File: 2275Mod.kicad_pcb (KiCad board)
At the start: 2 copper layers, 6 parts, among them J1 640388-8, J200 Conn_PIC_ICSP_ICD, K1 4052, K2 G5LE-14-CF_DC24, U1 LM340LAZ-5.0

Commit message: commit before starting kicad 7
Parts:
- added C1: .01/400v, Capacitor_THT:C_Rect_L10.0mm_W4.0mm_P7.50mm_MKS4, F.Cu at (118.2, 93.1)
- added C2: 1000uf, Capacitor_THT:CP_Radial_D16.0mm_P7.50mm, F.Cu at (146.6, 80.0)
- added C200: .1uf, Capacitor_SMD:C_0603_1608Metric_Pad1.08x0.95mm_HandSolder, F.Cu at (195.1, 97.0)
- added C201: 4700uf, Capacitor_THT:CP_Radial_D25.0mm_P10.00mm_SnapIn, F.Cu at (203.9, 114.8)
- added C3: 10uf, Capacitor_THT:CP_Radial_D5.0mm_P2.50mm, F.Cu at (187.5, 97.0)
- added D1: MRA4007T3G, Diode_SMD:D_SMA, F.Cu at (143.3, 100.6)
- added D200: LED, LED_SMD:LED_0603_1608Metric_Pad1.05x0.95mm_HandSolder, F.Cu at (188.5, 78.7)
- added D201: LED, LED_SMD:LED_0805_2012Metric_Pad1.15x1.40mm_HandSolder, F.Cu at (188.5, 83.1)
- added H1: MountingHole, MountingHole:MountingHole_3.7mm, F.Cu at (108.2, 122.4)
- added H2: MountingHole, MountingHole:MountingHole_3.7mm, F.Cu at (206.8, 96.8)
- added H3: MountingHole, MountingHole:MountingHole_3.7mm, F.Cu at (108.2, 77.7)
- added IC1: LTV-356T, AAA_JH:SOP254P675X220-4N, F.Cu at (135.9, 87.9)
- added J201: Conn_01x03_Male, Connector_PinHeader_2.54mm:PinHeader_1x03_P2.54mm_Vertical, F.Cu at (196.1, 80.5)
- added Q200: Q_NPN_Darlington_CBE, AAA_JH:TRANS_2SD1918_ROM-M, F.Cu at (205.5, 79.2)
- added Q201: Q_NPN_Darlington_CBE, AAA_JH:TRANS_2SD1918_ROM-M, F.Cu at (214.9, 79.2)
- added R1: 47, Resistor_SMD:R_0805_2012Metric_Pad1.20x1.40mm_HandSolder, F.Cu at (118.4, 88.4)
- added R2: 2.2k, Resistor_SMD:R_0603_1608Metric_Pad0.98x0.95mm_HandSolder, F.Cu at (126.9, 87.4)
- added R200: 2.2k, Resistor_SMD:R_0603_1608Metric_Pad0.98x0.95mm_HandSolder, F.Cu at (174.8, 85.9)
- added R201: 2.2k, Resistor_SMD:R_0603_1608Metric_Pad0.98x0.95mm_HandSolder, F.Cu at (174.5, 90.2)
- added R202: 470, Resistor_SMD:R_0805_2012Metric_Pad1.20x1.40mm_HandSolder, F.Cu at (183.6, 78.7)
- added R203: 2.2k, Resistor_SMD:R_0603_1608Metric_Pad0.98x0.95mm_HandSolder, F.Cu at (181.6, 94.0)
- added R204: 470, Resistor_SMD:R_0805_2012Metric_Pad1.20x1.40mm_HandSolder, F.Cu at (183.9, 83.3)
- added R205: 220, Resistor_SMD:R_0805_2012Metric_Pad1.20x1.40mm_HandSolder, F.Cu at (192.5, 113.8)
- added R3: 100k, Resistor_SMD:R_1206_3216Metric_Pad1.30x1.75mm_HandSolder, F.Cu at (118.4, 77.2)
- added R4: 100k, Resistor_SMD:R_1206_3216Metric_Pad1.30x1.75mm_HandSolder, F.Cu at (117.9, 82.5)
- added R5: 10k, Resistor_SMD:R_0603_1608Metric_Pad0.98x0.95mm_HandSolder, F.Cu at (141.5, 95.0)
- added R6: 470, Resistor_SMD:R_0603_1608Metric_Pad0.98x0.95mm_HandSolder, F.Cu at (152.1, 98.8)
- added U2: TCLT1600, AAA_JH:SOP254P1015X230-4N, F.Cu at (129.3, 74.9)
- added U200: PIC16F1613-I/SL, Package_SO:SOIC-14_3.9x8.7mm_P1.27mm, F.Cu at (171.4, 96.5)
- added U3: TCLT1600, AAA_JH:SOP254P1015X230-4N, F.Cu at (129.3, 81.3)
- added q1: NPN_Transistor, Package_TO_SOT_SMD:SOT-23-3, F.Cu at (147.3, 96.0)
- K1: value 4052 -> 40.52.8.024.5000
- moved K2 16.0 mm to (138.3, 123.7)
- moved K1 11.7 mm to (121.9, 93.1)
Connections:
- net Net-(C1-Pad2) renamed /L2
- J1 pad 3: /TEST -> TEST
- K1 pad 1: /L1 -> /UTIL
- K1 pad 5: Net-(K1-Pad5) -> /UTIL
- K2 pad 2: GND -> +24V
- K2 pad 4: Net-(K1-Pad5) -> /UTIL
- K2 pad 5: TEST -> Net-(D1-Pad1)

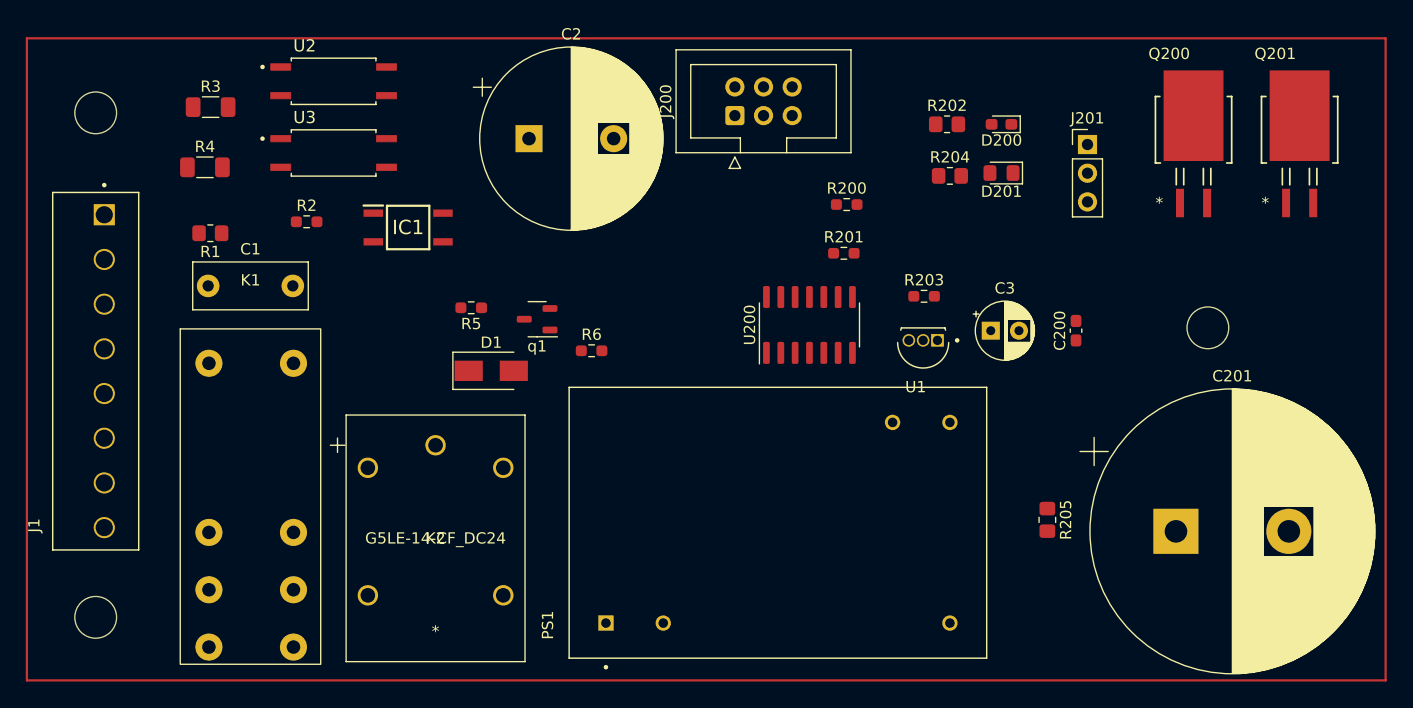
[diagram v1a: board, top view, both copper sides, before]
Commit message: move parts on the PCB
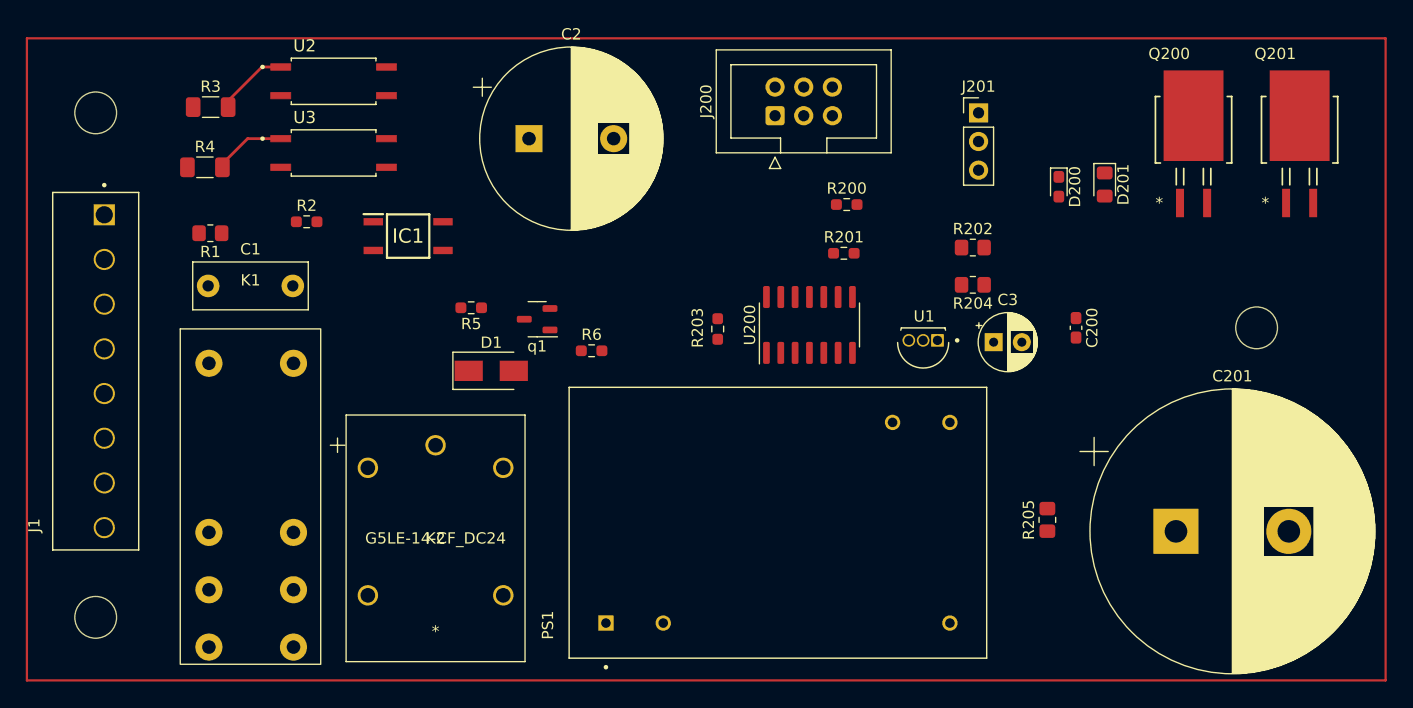
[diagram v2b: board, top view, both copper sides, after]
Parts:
- D200: value LED -> LED Yellow
- D201: value LED -> LED red
- moved R203 18.5 mm to (163.3, 96.9), turned to -90 degrees
- moved R202 11.2 mm to (185.9, 89.7)
- moved J201 10.1 mm to (186.4, 77.7)
- moved R204 9.86 mm to (185.9, 93.0), turned to 180 degrees
- moved D201 9.20 mm to (197.6, 84.1), turned to -90 degrees
- moved D200 7.51 mm to (193.5, 84.3), turned to -90 degrees
- moved H2 4.32 mm to (211.1, 96.8)
- moved J200 3.56 mm to (168.4, 78.0)
- moved C3 1.05 mm to (187.8, 98.0)
- moved IC1 0.76 mm to (135.9, 88.6)
- moved C200 0.25 mm to (195.1, 96.8), turned to -90 degrees
- turned R205 to 90 degrees
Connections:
- net Net-(J201-Pad1) renamed /MCU/Close
- net Net-(J201-Pad3) renamed /MCU/Open
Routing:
- net Net-(R3-Pad2): track 0.00 -> 6.46 mm
- net Net-(R4-Pad2): track 0.00 -> 6.40 mm

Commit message: board rearrange
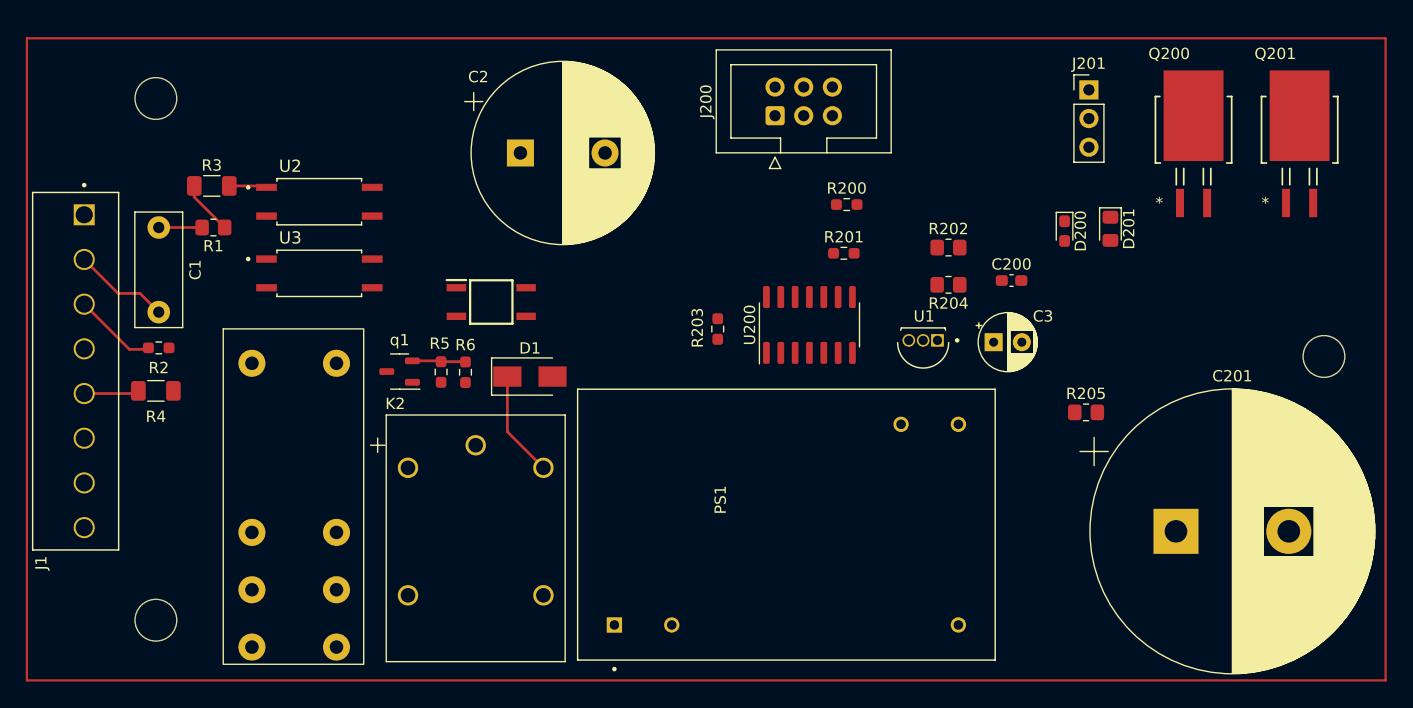
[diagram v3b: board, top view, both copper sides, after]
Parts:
- moved R4 20.3 mm to (113.5, 102.4)
- moved R2 17.2 mm to (113.8, 98.6)
- moved q1 13.0 mm to (135.1, 100.7)
- moved R6 11.3 mm to (141.0, 100.7), turned to -90 degrees
- moved U2 10.7 mm to (128.0, 85.6)
- moved U3 10.7 mm to (128.0, 91.9)
- moved R205 10.1 mm to (196.0, 104.3), turned to 0 degrees
- moved J201 9.99 mm to (196.2, 75.7)
- moved IC1 9.40 mm to (143.3, 94.5)
- moved C200 7.09 mm to (189.4, 92.6), turned to 0 degrees
- moved R3 6.99 mm to (118.5, 84.2)
- moved C1 6.78 mm to (113.8, 87.9), turned to -90 degrees
- moved H2 6.49 mm to (217.0, 99.3)
- moved R5 6.29 mm to (138.8, 100.7), turned to -90 degrees
- moved H3 5.48 mm to (113.5, 76.5)
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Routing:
- net Net-(D1-K): track 0.00 -> 9.41 mm
- net /L2: track 0.00 -> 8.54 mm
- net TEST: track 0.00 -> 7.40 mm
- net Net-(R4-Pad2): track 6.40 -> 0.00 mm
- net /G_L1: track 0.00 -> 4.90 mm
- net /UTIL: track 0.00 -> 4.80 mm
- net Net-(q1-B): track 0.00 -> 4.74 mm
- net Net-(C1-Pad1): track 0.00 -> 3.84 mm
- net Net-(R3-Pad2): track 6.46 -> 3.34 mm

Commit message: add test points, clean up errors
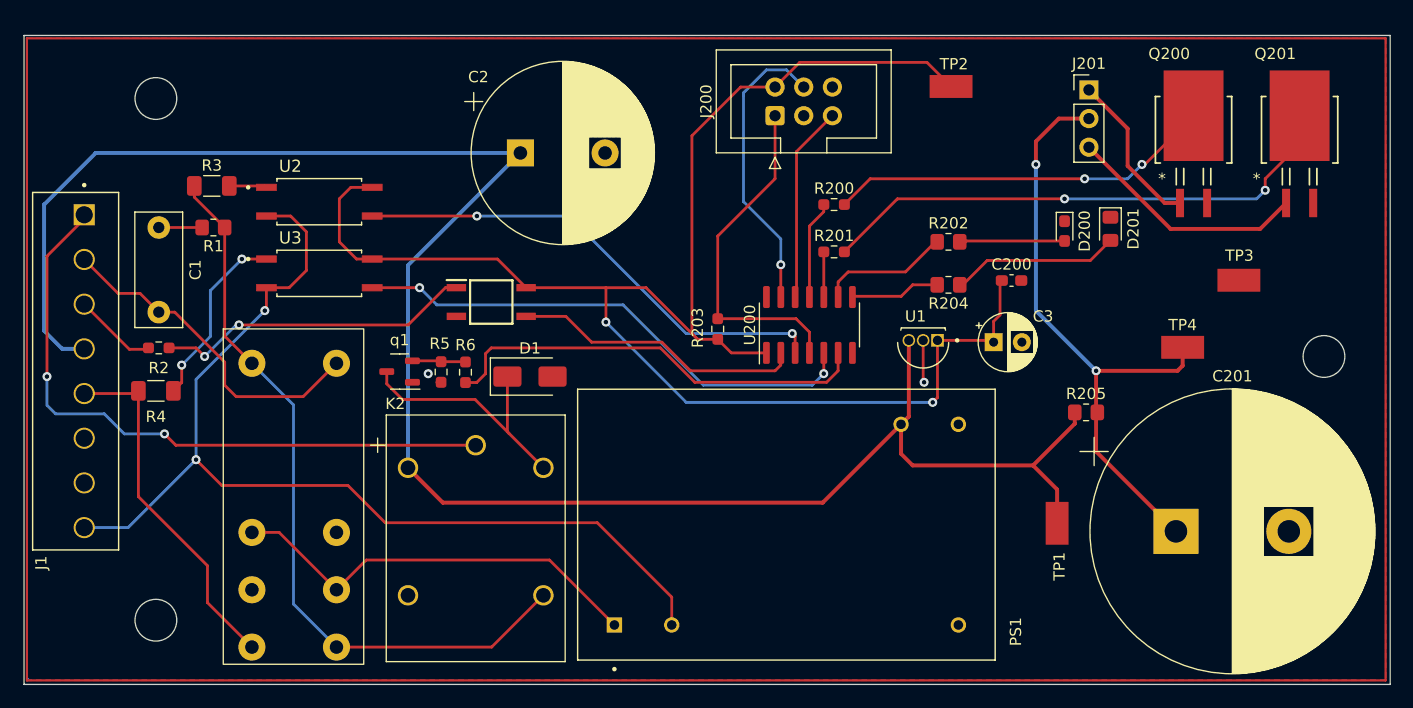
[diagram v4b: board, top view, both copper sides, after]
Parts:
- added TP1: 5019, AAA_Misc:KEYSTONE_5019, F.Cu at (193.4, 114.1)
- added TP2: 5019, AAA_Misc:KEYSTONE_5019, F.Cu at (184.0, 75.4)
- added TP3: 5019, AAA_Misc:KEYSTONE_5019, F.Cu at (209.5, 92.6)
- added TP4: 5019, AAA_Misc:KEYSTONE_5019, F.Cu at (204.5, 98.5)
- moved R200 1.12 mm to (173.6, 85.9)
- moved R201 0.87 mm to (173.6, 90.0)
- moved R202 0.51 mm to (183.8, 89.2)
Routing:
- net +24V: track 0.00 -> 174.1 mm
- net +5V: track 0.00 -> 145.3 mm, vias 0 -> 2
- net Earth: track 0.00 -> 91.6 mm, vias 0 -> 2
- net /UTIL: track 4.80 -> 66.3 mm
- net /L1: track 0.00 -> 57.7 mm, vias 0 -> 2
- net /MCU/BLP: track 0.00 -> 54.8 mm, vias 0 -> 2
- net Net-(Q201-B): track 0.00 -> 47.4 mm, vias 0 -> 2
- net GEN_sig: track 0.00 -> 45.9 mm, vias 0 -> 2
- net UTIL_sig: track 0.00 -> 43.4 mm, vias 0 -> 2
- net TEST_ON: track 0.00 -> 38.6 mm
- net Net-(PS1-VAC_IN(L)): track 0.00 -> 37.7 mm
- net Net-(Q200-B): track 0.00 -> 34.2 mm, vias 0 -> 2
- net /MCU/MCLR: track 0.00 -> 30.6 mm
- net Net-(IC1-ANODE): track 0.00 -> 28.3 mm, vias 0 -> 2
- net /G_L1: track 4.90 -> 31.8 mm
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- added copper zone on B.Cu, net GND
- added copper zone on F.Cu, net GND
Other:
- board outline added: 121.1 x 57.5 mm

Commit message: add test points, add open, close to connector on silk screen, add 3d model for the power supply part
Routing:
- net GND: vias 2 -> 12
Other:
- board text added: "CLOSE"
- board text added: "OPEN"
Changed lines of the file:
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@@
     )
     (pad_to_mask_clearance 0)
+    (aux_axis_origin 102.108 128.016)
     (pcbplotparams
       (layerselection 0x00010fc_ffffffff)
@@
       (drillshape 0)
       (scaleselection 1)
-      (outputdirectory "Gerber/")
+      (outputdirectory "Gerbers/")
     )
   )
@@
       )
     )
+    (model "/home/jeff/KiCad_libraries/STEP/RAC05E-24SK.step"
+      (offset (xyz 0 0 0))
+      (scale (xyz 1 1 1))
+      (rotate (xyz -90 0 90))
+    )
   )
   (footprint "LED_SMD:LED_0805_2012Metric_Pad1.15x1.40mm_HandSolder" (layer "F.Cu")
@@
   (gr_line (start 222.9104 70.866) (end 222.9104 128.3716)
     (stroke (width 0.1) (type default)) (layer "Edge.Cuts"))
+  (gr_text "OPEN" (at 190.246 81.3816) (layer "F.SilkS")
+    (effects (font (size 1 1) (thickness 0.15)) (justify left bottom))
+  )
+  (gr_text "CLOSE" (at 189.5348 76.0984) (layer "F.SilkS")
+    (effects (font (size 1 1) (thickness 0.15)) (justify left bottom))
+  )
   (segment (start 103.886 101.092) (end 103.886 90.424) (width 0.25) (layer "F.Cu") (net 1))
   (segment (start 141.8765 107.177602) (end 115.305602 107.177602) (width 0.25) (layer "F.Cu") (net 1))
@@
   (segment (start 181.52625 97.8855) (end 181.52625 101.51625) (width 0.25) (layer "F.Cu") (net 9))
   (via (at 137.668 100.838) (size 0.8) (drill 0.4) (layers "F.Cu" "B.Cu") (net 9))
+  (via (at 183.7944 80.1116) (size 0.8) (drill 0.4) (layers "F.Cu" "B.Cu") (free) (net 9))
+  (via (at 133.4008 76.0984) (size 0.8) (drill 0.4) (layers "F.Cu" "B.Cu") (free) (net 9))
+  (via (at 106.0196 119.9896) (size 0.8) (drill 0.4) (layers "F.Cu" "B.Cu") (free) (net 9))
+  (via (at 200.152 93.3704) (size 0.8) (drill 0.4) (layers "F.Cu" "B.Cu") (free) (net 9))
   (via (at 181.61 101.6) (size 0.8) (drill 0.4) (layers "F.Cu" "B.Cu") (net 9))
+  (via (at 168.91 118.364) (size 0.8) (drill 0.4) (layers "F.Cu" "B.Cu") (free) (net 9))
+  (via (at 106.172 77.6224) (size 0.8) (drill 0.4) (layers "F.Cu" "B.Cu") (free) (net 9))
+  (via (at 129.9972 104.1908) (size 0.8) (drill 0.4) (layers "F.Cu" "B.Cu") (free) (net 9))
+  (via (at 122.174 75.8952) (size 0.8) (drill 0.4) (layers "F.Cu" "B.Cu") (free) (net 9))
+  (via (at 219.6084 89.6112) (size 0.8) (drill 0.4) (layers "F.Cu" "B.Cu") (free) (net 9))
+  (via (at 157.7848 106.9848) (size 0.8) (drill 0.4) (layers "F.Cu" "B.Cu") (free) (net 9))
   (segment (start 135.382 103.124) (end 141.822896 103.124) (width 0.25) (layer "F.Cu") (net 10))
   (segment (start 133.996 101.738) (end 135.382 103.124) (width 0.25) (layer "F.Cu") (net 10))

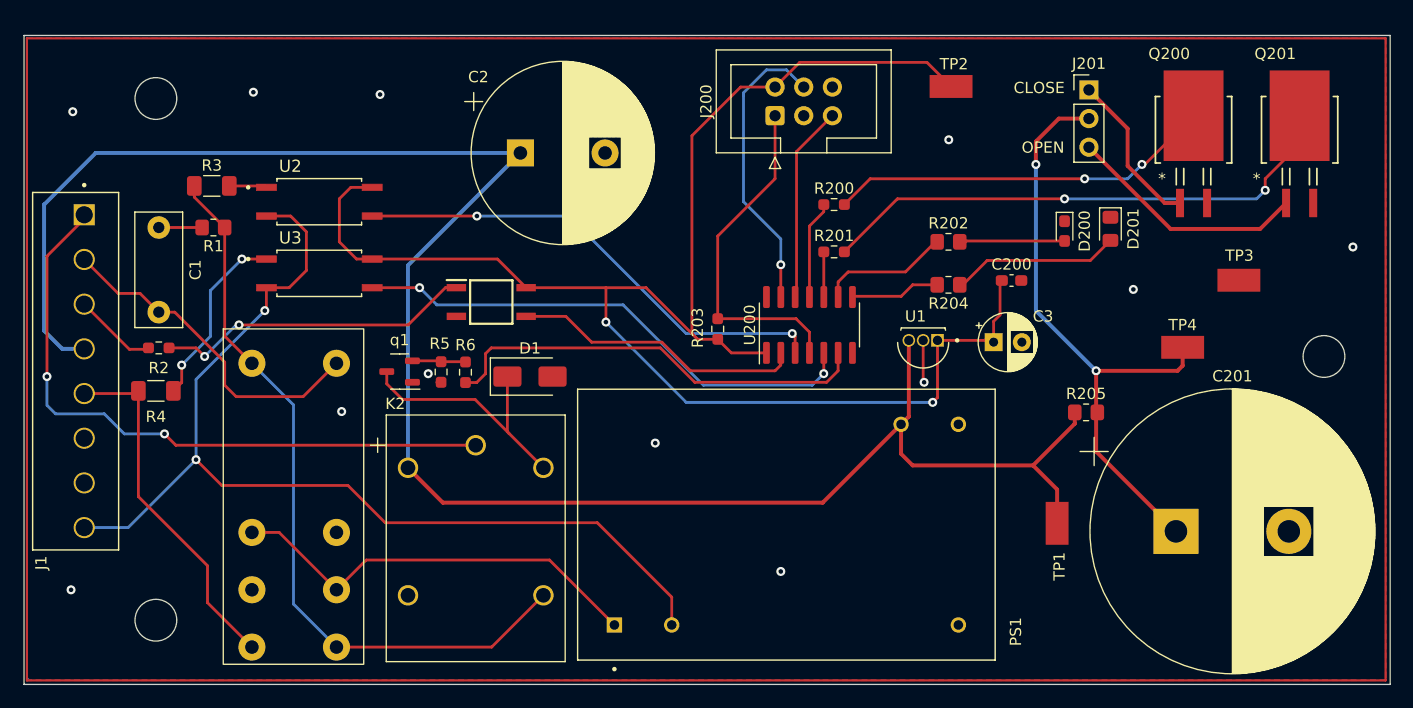
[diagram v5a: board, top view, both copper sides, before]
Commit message: make some traces thicker
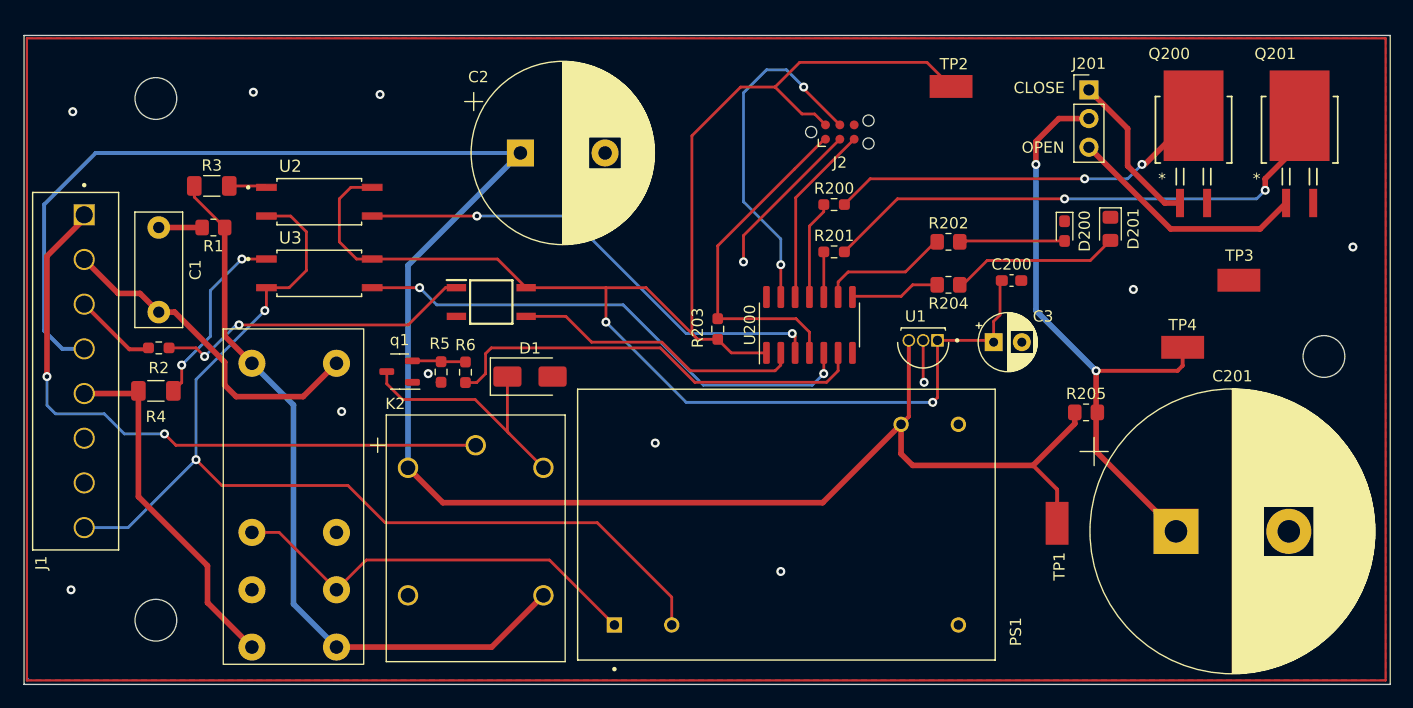
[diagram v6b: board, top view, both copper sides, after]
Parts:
- removed J200: Conn_PIC_ICSP_ICD, Connector_IDC:IDC-Header_2x03_P2.54mm_Vertical
- added J2: TagConnect_TC2030-MCP, Connector:Tag-Connect_TC2030-IDC-NL_2x03_P1.27mm_Vertical, F.Cu at (174.1, 79.4)
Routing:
- net GND: track 4.13 -> 18.5 mm
- net +5V: track 145.3 -> 151.1 mm
- net /MCU/DAT: track 26.3 -> 31.0 mm, vias 1 -> 2
- net /MCU/CLK: track 17.4 -> 16.2 mm
